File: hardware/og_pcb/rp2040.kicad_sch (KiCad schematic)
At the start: 29 parts, among them J11 Conn_02x02_Top_Bottom, J4 Micro_SD_Card_Det1, SW4 SW_Push_Shielded, SW5 SW_Push_Shielded, U12 RP2040, U3 W25Q128JVS, Y3 ABM8-272-T3

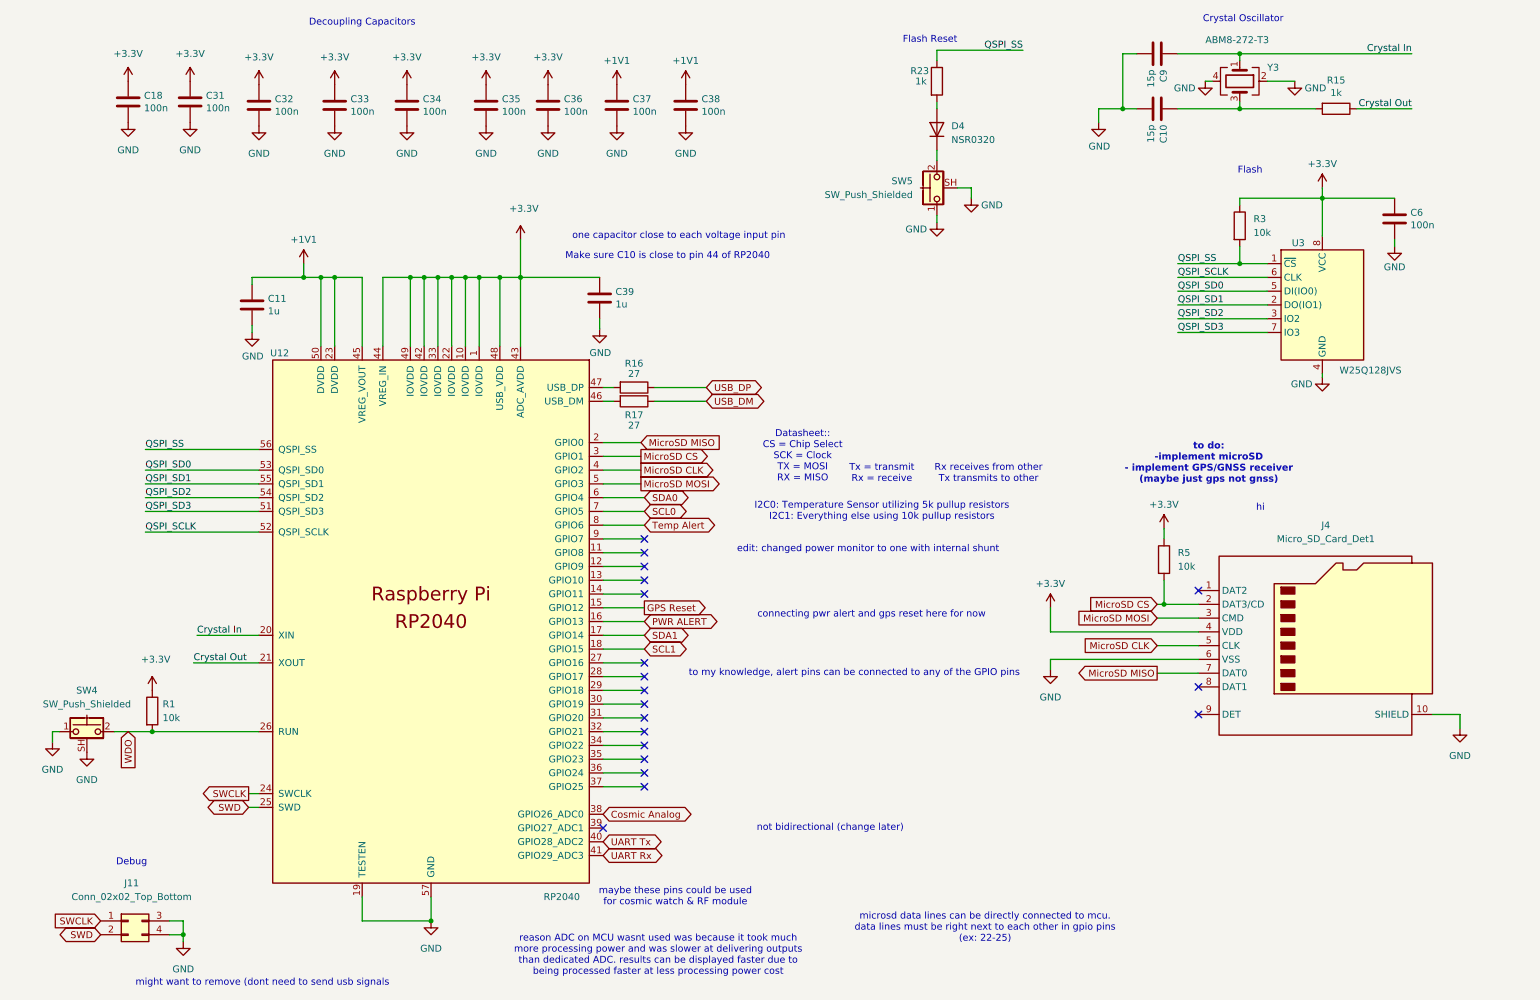
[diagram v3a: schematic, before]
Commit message: updated pcb
added footprints, led, testpoints
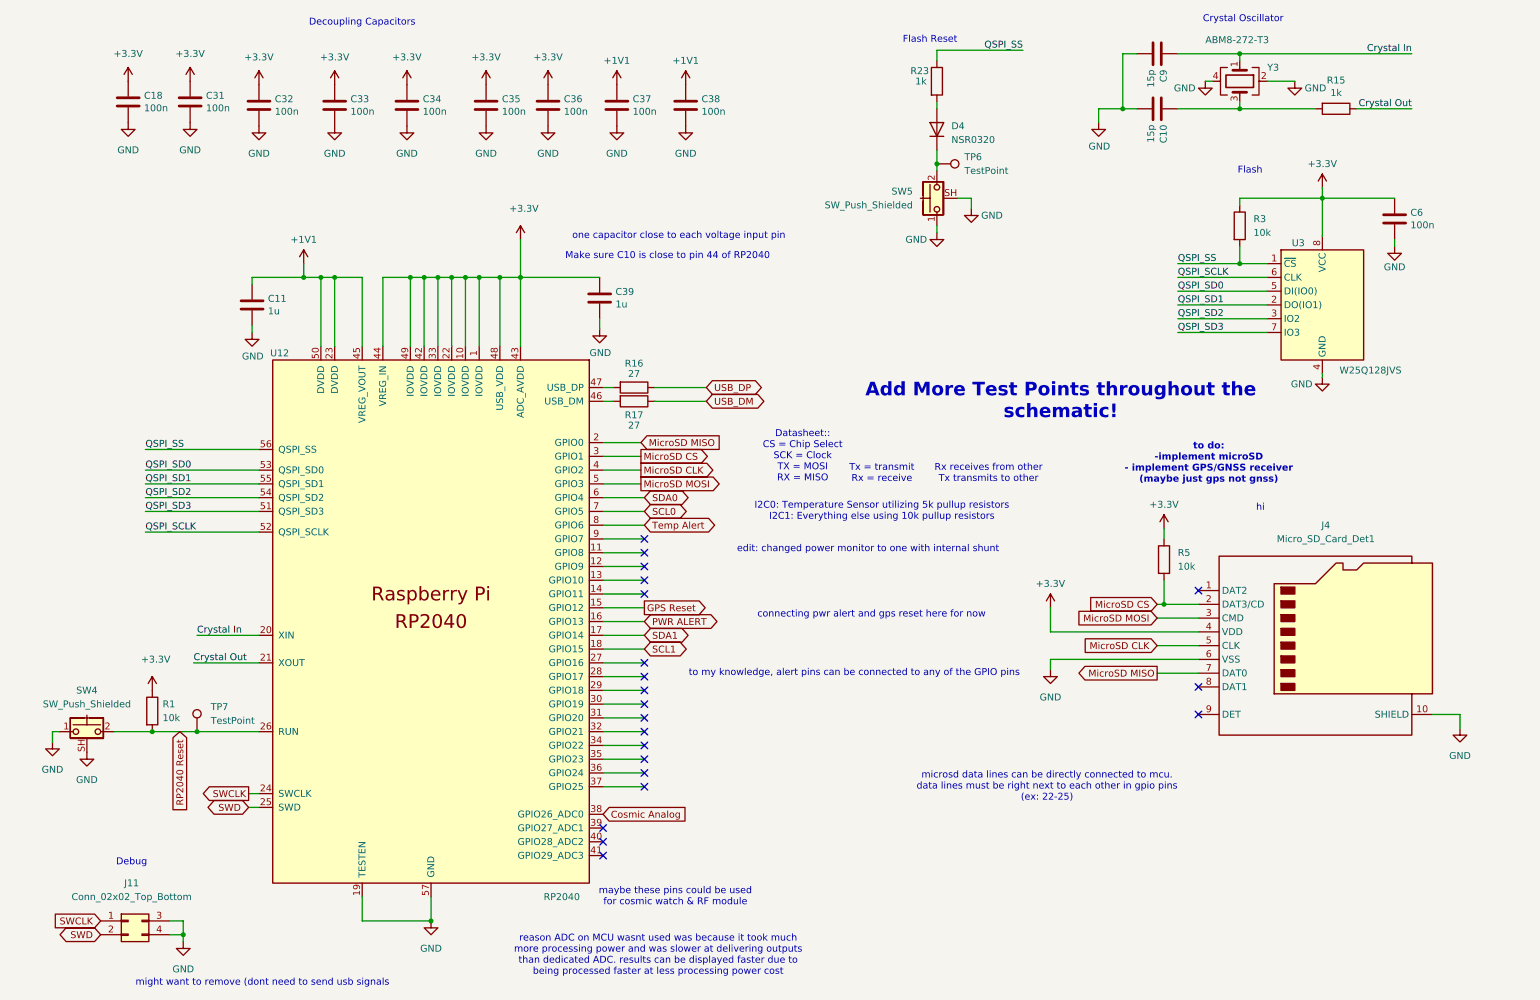
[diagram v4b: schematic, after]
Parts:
- added TP6, TP7: TestPoint, 1my_footprints:TestPoint_Loop_D1.80mm_Drill1.0mm_Beaded, symbol Connector:TestPoint
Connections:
- net at D4.1 (K), SW5.2: now also TP6.1
- net UART Rx: no longer names the net of U12.41 (GPIO29_ADC3)
- net UART Tx: no longer names the net of U12.40 (GPIO28_ADC2)
- net WDO renamed RP2040 Reset
- net RP2040 Reset: now also TP7.1
- no-connect marks 19 -> 21
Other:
- note added: "Add More Test Points throughout the schematic!"
- note removed: "not bidirectional (change later)"
- moved on the sheet: SW5

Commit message: pushed latest version
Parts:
- removed J11: Conn_02x02_Top_Bottom, 1my_footprints:CON4_2X2_UF_DF11_HIR, symbol Connector_Generic:Conn_02x02_Top_Bottom
- added J5: Conn_01x02_Pin, symbol Connector:Conn_01x02_Pin
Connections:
- net SWCLK: now also J5.2 (Pin_2)
- net SWD: now also J5.1 (Pin_1)
- net PWR ALERT: no longer names the net of U12.16 (GPIO13)
- net Temp Alert: no longer names the net of U12.8 (GPIO6)
- no-connect marks 21 -> 23
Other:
- note added: "27 ohm resistors should be placed close to the MCU"
- note added: "Serial Wire Debug (Male Header Pins)"
- note added: "change to male header pins"
- note added: "what is power alert again?"
- note removed: "Debug"

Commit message: added comments from pragun's review
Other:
- note added: "(old note from william)"
- note added: "(william's note)"
- note added: "look at what adafruit module uses: hc4050 buffer"
- note added: "look into buffer for sd card (SD card on proves kit pcb doesn't work)"
- note added: "look into if 12MHz will impact data processing of the cosmic watch data which is usually at 16HMz"
- note added: "make sure diode used is exactly same one as used in proves kit"
- note added: "make sure flash as close to RP2040 as possible"
- note removed: "Add More Test Points throughout the schematic!"
- note removed: "change to male header pins"
- note removed: "connecting pwr alert and gps reset here for now"
- note removed: "edit: changed power monitor to one with internal shunt"
- note removed: "maybe these pins could be used for cosmic watch & RF module"
- note removed: "might want to remove (dont need to send usb signals"
- note removed: "reason ADC on MCU wasnt used was because it took much more processing power and was slower at delivering outputs than dedicated ADC. results can be displayed faster due to being processed faster at less processing power cost"
- note removed: "to do: -implement microSD - implement GPS/GNSS receiver (maybe just gps not gnss)"
- note removed: "what is power alert again?"
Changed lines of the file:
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@@
 	(generator_version "9.0")
 	(paper "A4")
-	(text "to do:\n-implement microSD\n- implement GPS/GNSS receiver\n(maybe just gps not gnss)"
-		(exclude_from_sim no)
-		(at 229.235 99.695 0)
-		(effects
-			(font
-				(size 1.27 1.27)
-				(thickness 0.254)
-				(bold yes)
-			)
-		)
-	)
 	(text "Make sure C10 is close to pin 44 of RP2040"
 		(exclude_from_sim no)
@@
 			)
 			(justify left bottom)
+		)
+	)
+	(text "look into buffer for sd card\n(SD card on proves kit pcb doesn't work)"
+		(exclude_from_sim no)
+		(at 254.635 154.94 0)
+		(effects
+			(font
+				(size 1.27 1.27)
+			)
+		)
+	)
+	(text "look at what adafruit module uses:\nhc4050 buffer"
+		(exclude_from_sim no)
+		(at 260.35 161.925 0)
+		(effects
+			(font
+				(size 1.27 1.27)
+			)
+		)
+	)
+	(text "(william's note)"
+		(exclude_from_sim no)
+		(at 165.1 136.525 0)
+		(effects
+			(font
+				(size 1.27 1.27)
+			)
 		)
 	)
@@
 		)
 	)
-	(text "maybe these pins could be used \nfor cosmic watch & RF module"
-		(exclude_from_sim no)
-		(at 130.81 179.705 0)
-		(effects
-			(font
-				(size 1.27 1.27)
-			)
-		)
-	)
 	(text "Tx = transmit\nRx = receive"
 		(exclude_from_sim no)
 		(at 168.91 101.6 0)
-		(effects
-			(font
-				(size 1.27 1.27)
-			)
-		)
-	)
-	(text "edit: changed power monitor to one with internal shunt"
-		(exclude_from_sim no)
-		(at 166.37 115.57 0)
-		(effects
-			(font
-				(size 1.27 1.27)
-			)
-		)
-	)
-	(text "what is power alert again?"
-		(exclude_from_sim no)
-		(at 155.575 130.81 0)
 		(effects
 			(font
@@
 		)
 	)
-	(text "reason ADC on MCU wasnt used was because it took much\nmore processing power and was slower at delivering outputs\nthan dedicated ADC. results can be displayed faster due to\nbeing processed faster at less processing power cost"
+	(text "make sure flash as close to RP2040 as possible"
 		(exclude_from_sim no)
-		(at 127.635 190.5 0)
+		(at 260.35 87.63 0)
 		(effects
 			(font
 				(size 1.27 1.27)
-			)
-		)
-	)
-	(text "Add More Test Points throughout the \nschematic!"
-		(exclude_from_sim no)
-		(at 201.93 88.265 0)
-		(effects
-			(font
-				(size 2.5 2.5)
-				(thickness 0.338)
-				(bold yes)
 			)
 		)
@@
 		)
 	)
-	(text "connecting pwr alert and gps reset here for now"
+	(text "microsd data lines can be directly connected to mcu.\ndata lines must be right next to each other in gpio pins\n(ex: 22-25)"
 		(exclude_from_sim no)
-		(at 167.005 127.635 0)
+		(at 199.39 159.385 0)
 		(effects
 			(font
 				(size 1.27 1.27)
-				(thickness 0.1588)
 			)
 		)
 	)
-	(text "microsd data lines can be directly connected to mcu.\ndata lines must be right next to each other in gpio pins\n(ex: 22-25)"
+	(text "look into if 12MHz will impact data processing of\nthe cosmic watch data which is usually at 16HMz"
 		(exclude_from_sim no)
-		(at 199.39 159.385 0)
+		(at 249.555 39.37 0)
 		(effects
 			(font
@@
 		)
 	)
-	(text "might want to remove (dont need to send usb signals"
+	(text "make sure diode used is\nexactly same one as used in proves kit"
 		(exclude_from_sim no)
-		(at 54.61 195.58 0)
+		(at 156.21 38.735 0)
 		(effects
 			(font
@@
 		)
 	)
-	(text "change to male header pins"
+	(text "(old note from william)"
 		(exclude_from_sim no)
-		(at 47.625 189.23 0)
+		(at 199.39 154.305 0)
 		(effects
 			(font

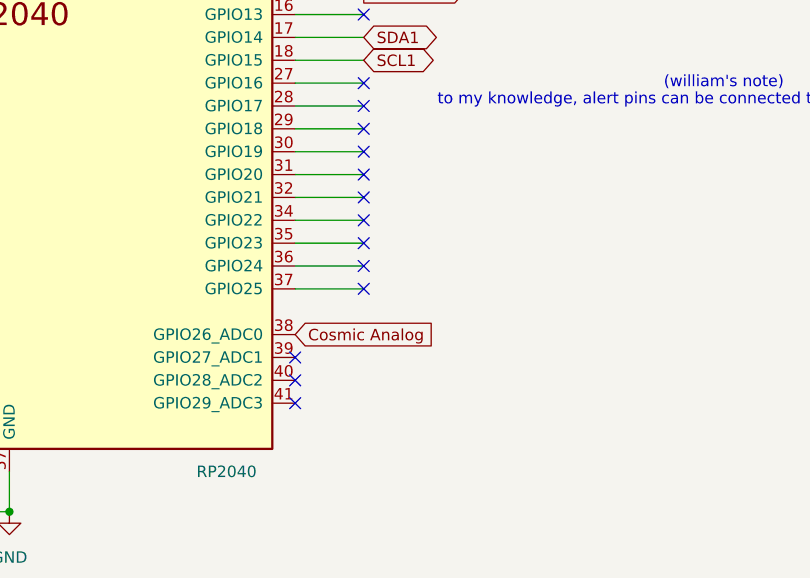
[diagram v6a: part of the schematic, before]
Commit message: implemented pragun's advice
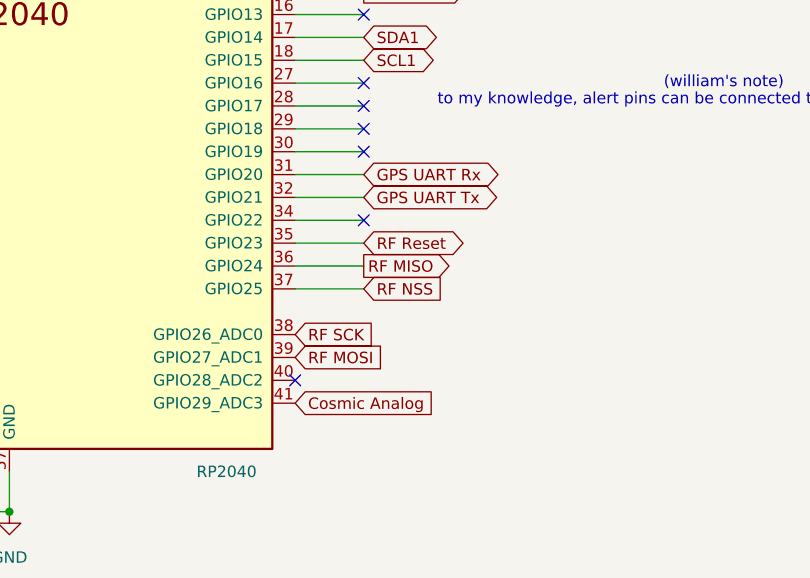
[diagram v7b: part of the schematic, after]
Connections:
- net Cosmic Analog: now also U12.41 (GPIO29_ADC3); no longer U12.38 (GPIO26_ADC0)
- net GPS UART Rx: now reaches U12.31 (GPIO20)
- net GPS UART Tx: now reaches U12.32 (GPIO21)
- net RF Reset: now reaches U12.35 (GPIO23)
- net RF MISO: now reaches U12.36 (GPIO24)
- net RF NSS: now reaches U12.37 (GPIO25)
- net RF MOSI: now reaches U12.39 (GPIO27_ADC1)
- new net RF SCK: U12.38 (GPIO26_ADC0)
- no-connect marks 23 -> 16
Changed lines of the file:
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@@
-	)
-	(no_connect
-		(at 125.095 154.305)
 	)
 	(no_connect
@@
 	)
 	(no_connect
-		(at 125.095 149.225)
-	)
-	(no_connect
-		(at 125.095 159.385)
-	)
-	(no_connect
 		(at 117.475 169.545)
 	)
@@
 	)
 	(no_connect
-		(at 125.095 146.685)
-	)
-	(no_connect
-		(at 117.475 172.085)
-	)
-	(no_connect
 		(at 125.095 113.665)
 	)
@@
 	)
 	(no_connect
-		(at 117.475 167.005)
-	)
-	(no_connect
 		(at 125.095 136.525)
 	)
@@
 	)
 	(no_connect
-		(at 125.095 156.845)
-	)
-	(no_connect
 		(at 125.095 128.905)
 	)
@@
 			)
 			(justify left bottom)
+		)
+	)
+	(global_label "GPS UART Tx"
+		(shape bidirectional)
+		(at 125.095 149.225 0)
+		(fields_autoplaced yes)
+		(effects
+			(font
+				(size 1.27 1.27)
+			)
+			(justify left)
+		)
+		(property "Intersheetrefs" "${INTERSHEET_REFS}"
+			(at 141.5286 149.225 0)
+			(effects
+				(font
+					(size 1.27 1.27)
+				)
+				(justify left)
+				(hide yes)
+			)
 		)
 	)
@@
 		)
 	)
+	(global_label "RF SCK"
+		(shape input)
+		(at 117.475 164.465 0)
+		(fields_autoplaced yes)
+		(effects
+			(font
+				(size 1.27 1.27)
+			)
+			(justify left)
+		)
+		(property "Intersheetrefs" "${INTERSHEET_REFS}"
+			(at 127.5359 164.465 0)
+			(effects
+				(font
+					(size 1.27 1.27)
+				)
+				(justify left)
+				(hide yes)
+			)
+		)
+	)
 	(global_label "SDA1"
 		(shape bidirectional)
@@
 		)
 	)
-	(global_label "Cosmic Analog"
-		(shape input)
-		(at 117.475 164.465 0)
-		(fields_autoplaced yes)
-		(effects
-			(font
-				(size 1.27 1.27)
-			)
-			(justify left)
-		)
-		(property "Intersheetrefs" "${INTERSHEET_REFS}"
-			(at 134.6114 164.465 0)
-			(effects
-				(font
-					(size 1.27 1.27)
-				)
-				(justify left)
-				(hide yes)
-			)
-		)
-	)
 	(global_label "MicroSD CS"
 		(shape input)
@@
 		)
 	)
+	(global_label "RF Reset"
+		(shape bidirectional)
+		(at 125.095 154.305 0)
+		(fields_autoplaced yes)
+		(effects
+			(font
+				(size 1.27 1.27)
+			)
+			(justify left)
+		)
+		(property "Intersheetrefs" "${INTERSHEET_REFS}"
+			(at 137.7187 154.305 0)
+			(effects
+				(font
+					(size 1.27 1.27)
+				)
+				(justify left)
+				(hide yes)
+			)
+		)
+	)
 	(global_label "MicroSD CLK"
 		(shape input)
@@
 		)
 	)
+	(global_label "RF MISO"
+		(shape output)
+		(at 125.095 156.845 0)
+		(fields_autoplaced yes)
+		(effects
+			(font
+				(size 1.27 1.27)
+			)
+			(justify left)
+		)
+		(property "Intersheetrefs" "${INTERSHEET_REFS}"
+			(at 136.0026 156.845 0)
+			(effects
+				(font
+					(size 1.27 1.27)
+				)
+				(justify left)
+				(hide yes)
+			)
+		)
+	)
 	(global_label "SDA0"
 		(shape bidirectional)
@@
 		)
 	)
+	(global_label "RF MOSI"
+		(shape input)
+		(at 117.475 167.005 0)
+		(fields_autoplaced yes)
+		(effects
+			(font
+				(size 1.27 1.27)
+			)
+			(justify left)
+		)
+		(property "Intersheetrefs" "${INTERSHEET_REFS}"
+			(at 128.3826 167.005 0)
+			(effects
+				(font
+					(size 1.27 1.27)
+				)
+				(justify left)
+				(hide yes)
+			)
+		)
+	)
 	(global_label "SWD"
 		(shape bidirectional)
@@
 		)
 	)
+	(global_label "GPS UART Rx"
+		(shape bidirectional)
+		(at 125.095 146.685 0)
+		(fields_autoplaced yes)
+		(effects
+			(font
+				(size 1.27 1.27)
+			)
+			(justify left)
+		)
+		(property "Intersheetrefs" "${INTERSHEET_REFS}"
+			(at 141.831 146.685 0)
+			(effects
+				(font
+					(size 1.27 1.27)
+				)
+				(justify left)
+				(hide yes)
+			)
+		)
+	)
 	(global_label "MicroSD MISO"
 		(shape input)
@@
 			(effects
 				(font
+					(size 1.27 1.27)
+				)
+				(justify left)
+				(hide yes)
+			)
+		)
+	)
+	(global_label "RF NSS"
+		(shape input)
+		(at 125.095 159.385 0)
+		(fields_autoplaced yes)
+		(effects
+			(font
+				(size 1.27 1.27)
+			)
+			(justify left)
+		)
+		(property "Intersheetrefs" "${INTERSHEET_REFS}"
+			(at 135.1559 159.385 0)
+			(effects
+				(font
+					(size 1.27 1.27)
+				)
+				(justify left)
+				(hide yes)
+			)
+		)
+	)
+	(global_label "Cosmic Analog"
+		(shape input)
+		(at 117.475 172.085 0)
+		(fields_autoplaced yes)
+		(effects
+			(font
+				(size 1.27 1.27)
+			)
+			(justify left)
+		)
+		(property "Intersheetrefs" "${INTERSHEET_REFS}"
+			(at 134.6114 172.085 0)
+			(effects
+				(font
